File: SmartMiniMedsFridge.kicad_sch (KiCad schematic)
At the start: 47 parts, among them J2 XHB-6AW, J3 Qwiic I2C, J4 Stemma I2C, U2 ESP32-S3-WROOM-1, U3 LMV321, U4 MPR121QR2, U5 SSD1306, U6 ESP32-C6-WROOM-1

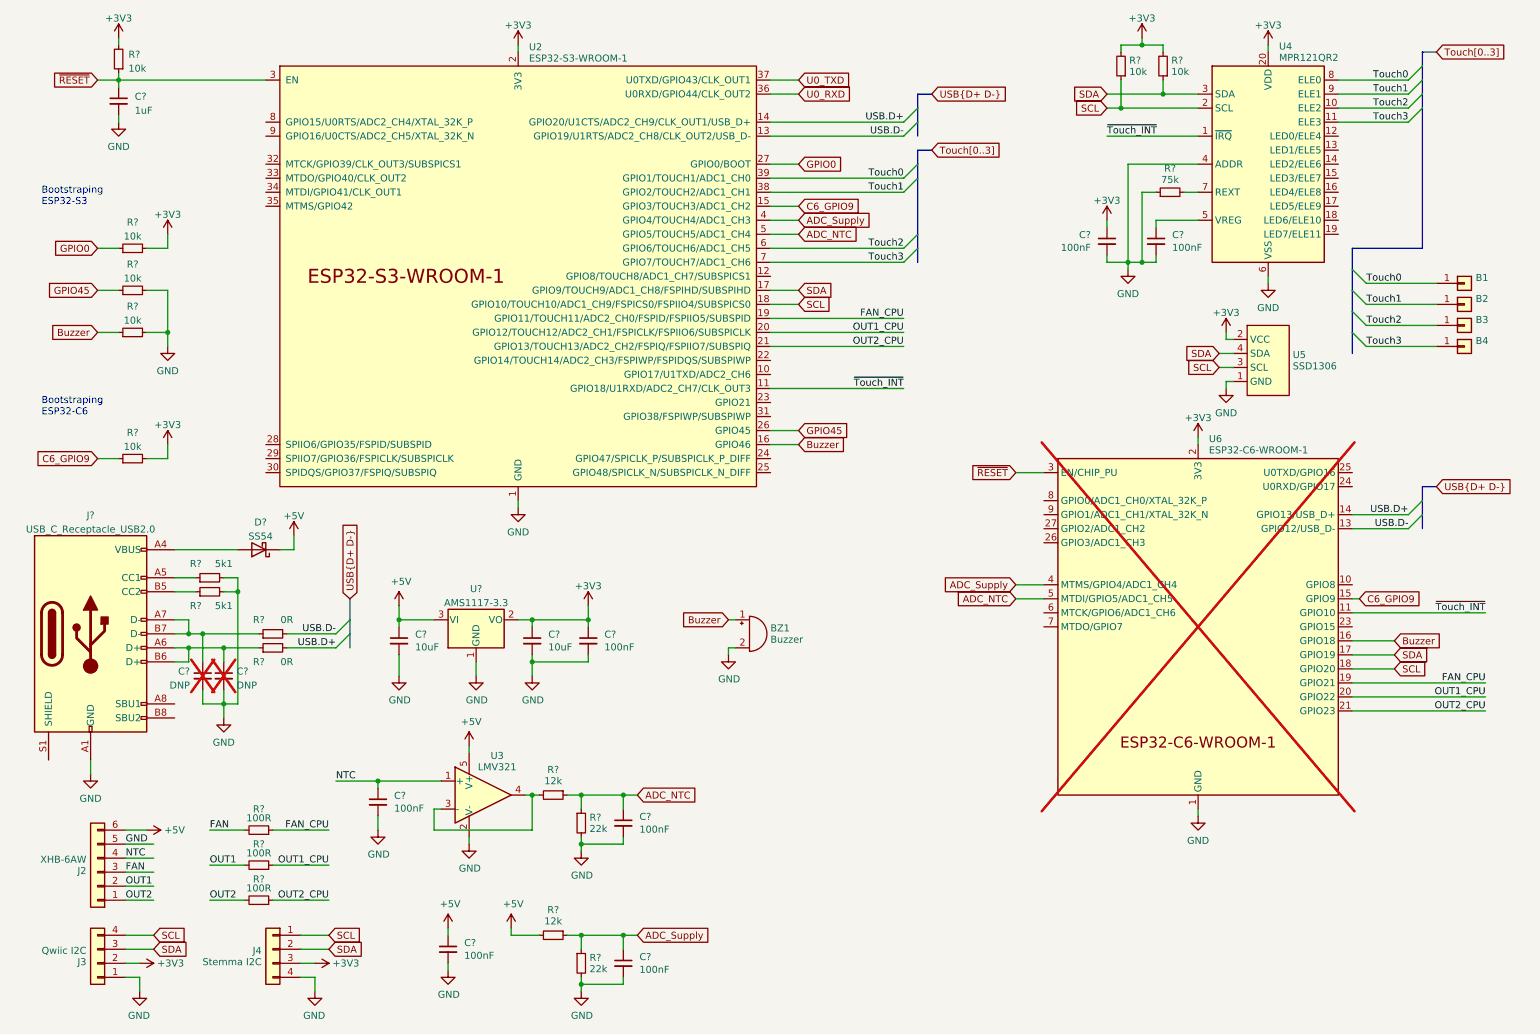
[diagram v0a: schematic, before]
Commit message: pre re-arrangement because of collision with case
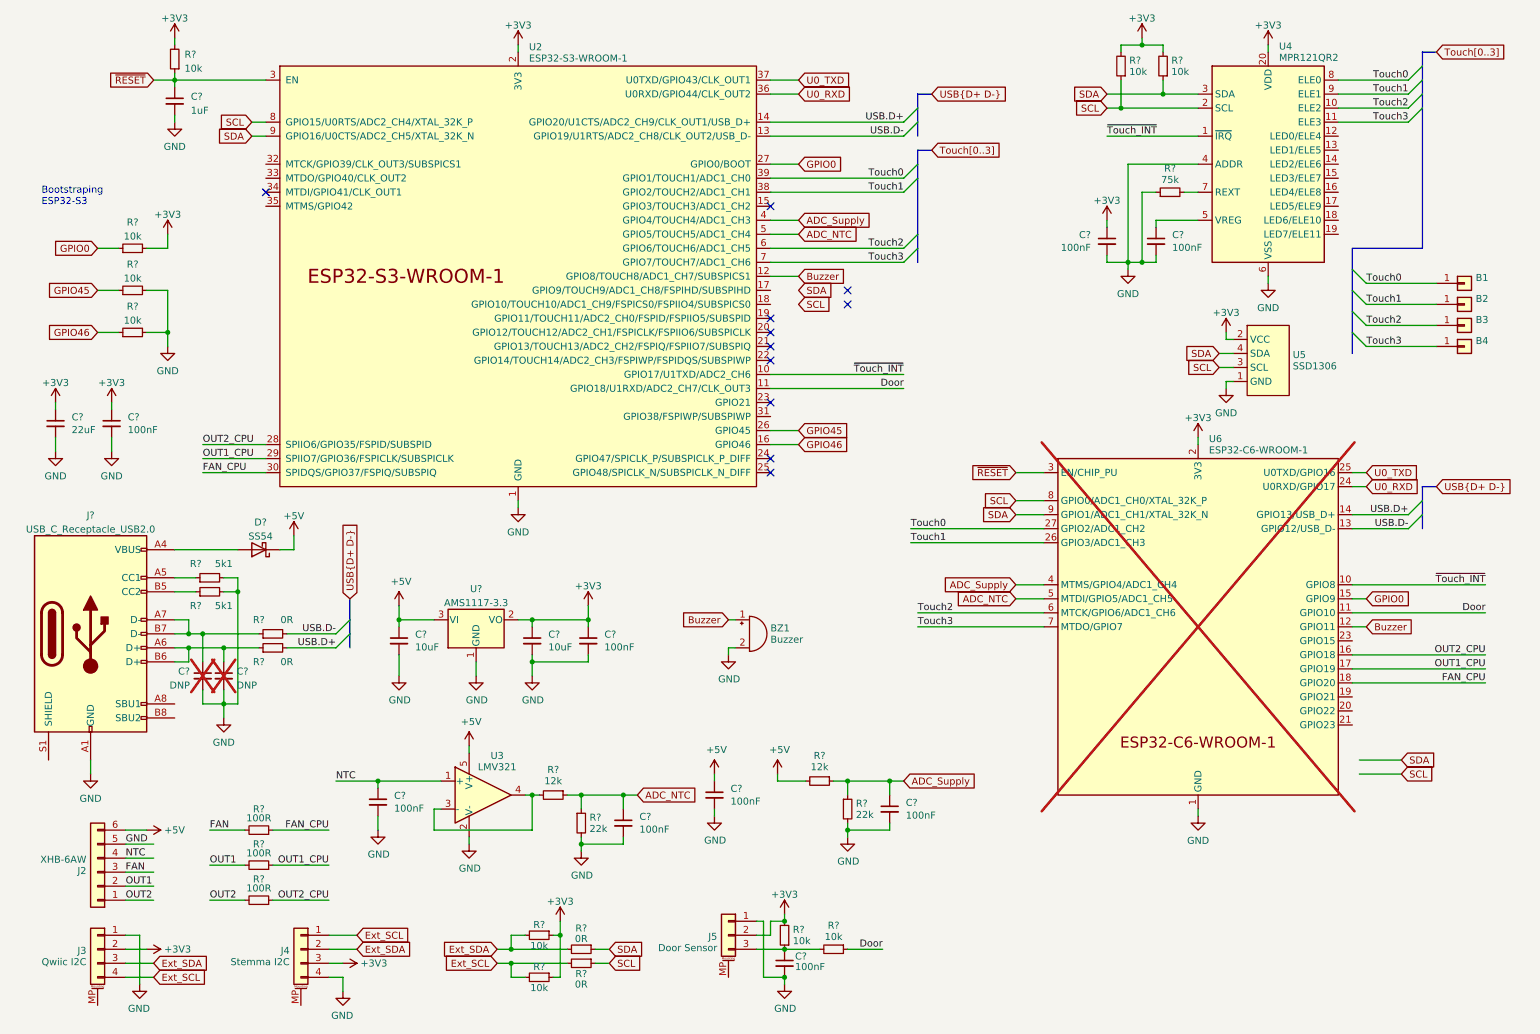
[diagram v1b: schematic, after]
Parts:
- added C?: 22uF, Capacitor_SMD:C_0603_1608Metric, symbol Device:C_Small
- added C? (x2): 100nF, Capacitor_SMD:C_0603_1608Metric, symbol Device:C_Small
- added J5: Door Sensor, Connector_JST:JST_PH_S3B-PH-SM4-TB_1x03-1MP_P2.00mm_Horizontal, symbol Connector_Generic_MountingPin:Conn_01x03_MountingPin
- added R? (x2): 0R, Resistor_SMD:R_0603_1608Metric, symbol Device:R_Small
- added R? (x3): 10k, Resistor_SMD:R_0603_1608Metric, symbol Device:R_Small
- B1, B2, B3, B4: value Conn_01x01 -> Spring Contact; LCSC (none) -> C5143801
- BZ1: LCSC (none) -> C76871
- J3, J4: symbol Connector_Generic:Conn_01x04 -> Connector_Generic_MountingPin:Conn_01x04_MountingPin
- U2: footprint PCM_Espressif:ESP32-S3-WROOM-1 -> Espressif:ESP32-S3-WROOM-1; symbol PCM_Espressif:ESP32-S3-WROOM-1 -> Espressif:ESP32-S3-WROOM-1
- U6: symbol PCM_Espressif:ESP32-C6-WROOM-1 -> Espressif:ESP32-C6-WROOM-1; now in the parts list
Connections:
- net +3V3: now also R?.1, C?.1, C?.1, J5.2 (Pin_2), R?.1, R?.2; no longer R?.2
- net Buzzer: now also U2.12 (GPIO8/TOUCH8/ADC1_CH7/SUBSPICS1), U6.12 (GPIO11); no longer R?.1, U2.16 (GPIO46), U6.16 (GPIO18)
- net FAN_CPU: now also U2.30 (SPIDQS/GPIO37/FSPIQ/SUBSPIQ), U6.18 (GPIO20); no longer U2.19 (GPIO11/TOUCH11/ADC2_CH0/FSPID/FSPIIO5/SUBSPID), U6.19 (GPIO21)
- net GND: now also C?.2, C?.2, C?.2, J5.1 (Pin_1); no longer U6.12 (GPIO11)
- net GPIO0: now also U6.15 (GPIO9)
- net OUT1_CPU: now also U2.29 (SPIIO7/GPIO36/FSPICLK/SUBSPICLK), U6.17 (GPIO19); no longer U2.20 (GPIO12/TOUCH12/ADC2_CH1/FSPICLK/FSPIIO6/SUBSPICLK), U6.20 (GPIO22)
- net OUT2_CPU: now also U2.28 (SPIIO6/GPIO35/FSPID/SUBSPID), U6.16 (GPIO18); no longer U2.21 (GPIO13/TOUCH13/ADC2_CH2/FSPIQ/FSPIIO7/SUBSPIQ), U6.21 (GPIO23)
- net SCL: now also U2.8 (GPIO15/U0RTS/ADC2_CH4/XTAL_32K_P), U6.8 (GPIO0/ADC1_CH0/XTAL_32K_P), R?.1; no longer J3.4 (Pin_4), J4.1 (Pin_1), U2.18 (GPIO10/TOUCH10/ADC1_CH9/FSPICS0/FSPIIO4/SUBSPICS0), U6.18 (GPIO20)
- net SDA: now also U2.9 (GPIO16/U0CTS/ADC2_CH5/XTAL_32K_N), U6.9 (GPIO1/ADC1_CH1/XTAL_32K_N), R?.1; no longer J3.3 (Pin_3), J4.2 (Pin_2), U2.17 (GPIO9/TOUCH9/ADC1_CH8/FSPIHD/SUBSPIHD), U6.17 (GPIO19)
- net Touch0: now also U6.27 (GPIO2/ADC1_CH2)
- net Touch1: now also U6.26 (GPIO3/ADC1_CH3)
- net Touch2: now also U6.6 (MTCK/GPIO6/ADC1_CH6)
- net Touch3: now also U6.7 (MTDO/GPIO7)
- net U0_RXD: now also U6.24 (U0RXD/GPIO17)
- net U0_TXD: now also U6.25 (U0TXD/GPIO16)
- net ~{Touch_INT}: now also U2.10 (GPIO17/U1TXD/ADC2_CH6), U6.10 (GPIO8); no longer U2.11 (GPIO18/U1RXD/ADC2_CH7/CLK_OUT3), U6.11 (GPIO10)
- removed net C6_GPIO9: R?.1, U2.15 (GPIO3/TOUCH3/ADC1_CH2), U6.15 (GPIO9)
- new net: C?.1, J5.3 (Pin_3), R?.1, R?.2
- new net Door: R?.1, U2.11 (GPIO18/U1RXD/ADC2_CH7/CLK_OUT3), U6.11 (GPIO10)
- new net Ext_SCL: J3.4 (Pin_4), J4.1 (Pin_1), R?.2, R?.2
- new net Ext_SDA: J3.3 (Pin_3), J4.2 (Pin_2), R?.2, R?.2
- new net GPIO46: R?.1, U2.16 (GPIO46)
- no-connect marks 0 -> 11
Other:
- note removed: "Bootstraping ESP32-C6"
- moved on the sheet: C?, R?

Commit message: 1st production version
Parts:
- added D2: White, LED_SMD:LED_0603_1608Metric, symbol Device:LED_Small
- added D3: Red, LED_SMD:LED_0603_1608Metric, symbol Device:LED_Small
- added J6: UART, Connector_PinHeader_2.54mm:PinHeader_1x06_P2.54mm_Vertical, symbol Connector_Generic:Conn_01x06
- added R? (x2): 1k, Resistor_SMD:R_0603_1608Metric, symbol Device:R_Small
- added R?: 100R, Resistor_SMD:R_0603_1608Metric, symbol Device:R_Small
- added SW1: Reset, Button_Switch_SMD:SW_Push_1P1T-SH_NO_CK_KMR2xxG, symbol Switch:SW_Push
- J?: footprint Connector_USB:USB_C_Receptacle_G-Switch_GT-USB-7010ASV -> Connector_USB:USB_C_Receptacle_G-Switch_GT-USB-7051x; LCSC C2760486 -> C2843970
- U4: renamed from U6; now left out of the parts list
- renumbered U3 to U2, U2 to U3, U4 to U5, U5 to U6
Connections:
- net +3V3: now also J6.3 (Pin_3), R?.2
- net Ext_SCL: now also U3.25 (GPIO48/SPICLK_N/SUBSPICLK_N_DIFF)
- net Ext_SDA: now also U3.24 (GPIO47/SPICLK_P/SUBSPICLK_P_DIFF)
- net GND: now also J3.MP (MountPin), J4.MP (MountPin), J5.MP (MountPin), J?.S1 (SHIELD), D2.1 (K), D3.1 (K), J6.1 (Pin_1), SW1.2, SW1.SH (Shield)
- net GPIO0: now also R?.1
- net SCL: now also U3.9 (GPIO16/U0CTS/ADC2_CH5/XTAL_32K_N), U4.9 (GPIO1/ADC1_CH1/XTAL_32K_N); no longer U3.8 (GPIO15/U0RTS/ADC2_CH4/XTAL_32K_P), U4.8 (GPIO0/ADC1_CH0/XTAL_32K_P)
- net SDA: now also U3.8 (GPIO15/U0RTS/ADC2_CH4/XTAL_32K_P), U4.8 (GPIO0/ADC1_CH0/XTAL_32K_P); no longer U3.9 (GPIO16/U0CTS/ADC2_CH5/XTAL_32K_N), U4.9 (GPIO1/ADC1_CH1/XTAL_32K_N)
- net U0_RXD: now also J6.4 (Pin_4)
- net U0_TXD: now also J6.5 (Pin_5)
- net ~{RESET}: now also J6.2 (Pin_2), SW1.1
- net GPIO38: now reaches U3.31 (GPIO38/FSPIWP/SUBSPIWP)
- net GPIO38: now also U4.19 (GPIO21), R?.2
- net GPIO39: now reaches U3.32 (MTCK/GPIO39/CLK_OUT3/SUBSPICS1)
- net GPIO39: now also U4.20 (GPIO22)
- net GPIO40: now reaches U3.33 (MTDO/GPIO40/CLK_OUT2)
- net GPIO40: now also U4.21 (GPIO23)
- net GPIO42: now reaches U3.35 (MTMS/GPIO42)
- net GPIO42: now also U4.23 (GPIO15)
- new net: D3.2 (A), R?.1
- new net: D2.2 (A), R?.1
- new net: J6.6 (Pin_6), R?.2
- no-connect marks 11 -> 9
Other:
- moved on the sheet: BZ1, J2, J3, J4, R?
